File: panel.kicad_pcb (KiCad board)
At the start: 2 copper layers, 184.8 x 134.8 mm, 316 parts, among them J1 JST_SH_SM06B-SRSS-TB_1x06-1MP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, SW1 SW_Push, SW2 SW_Push, U1 M24C02-FMN

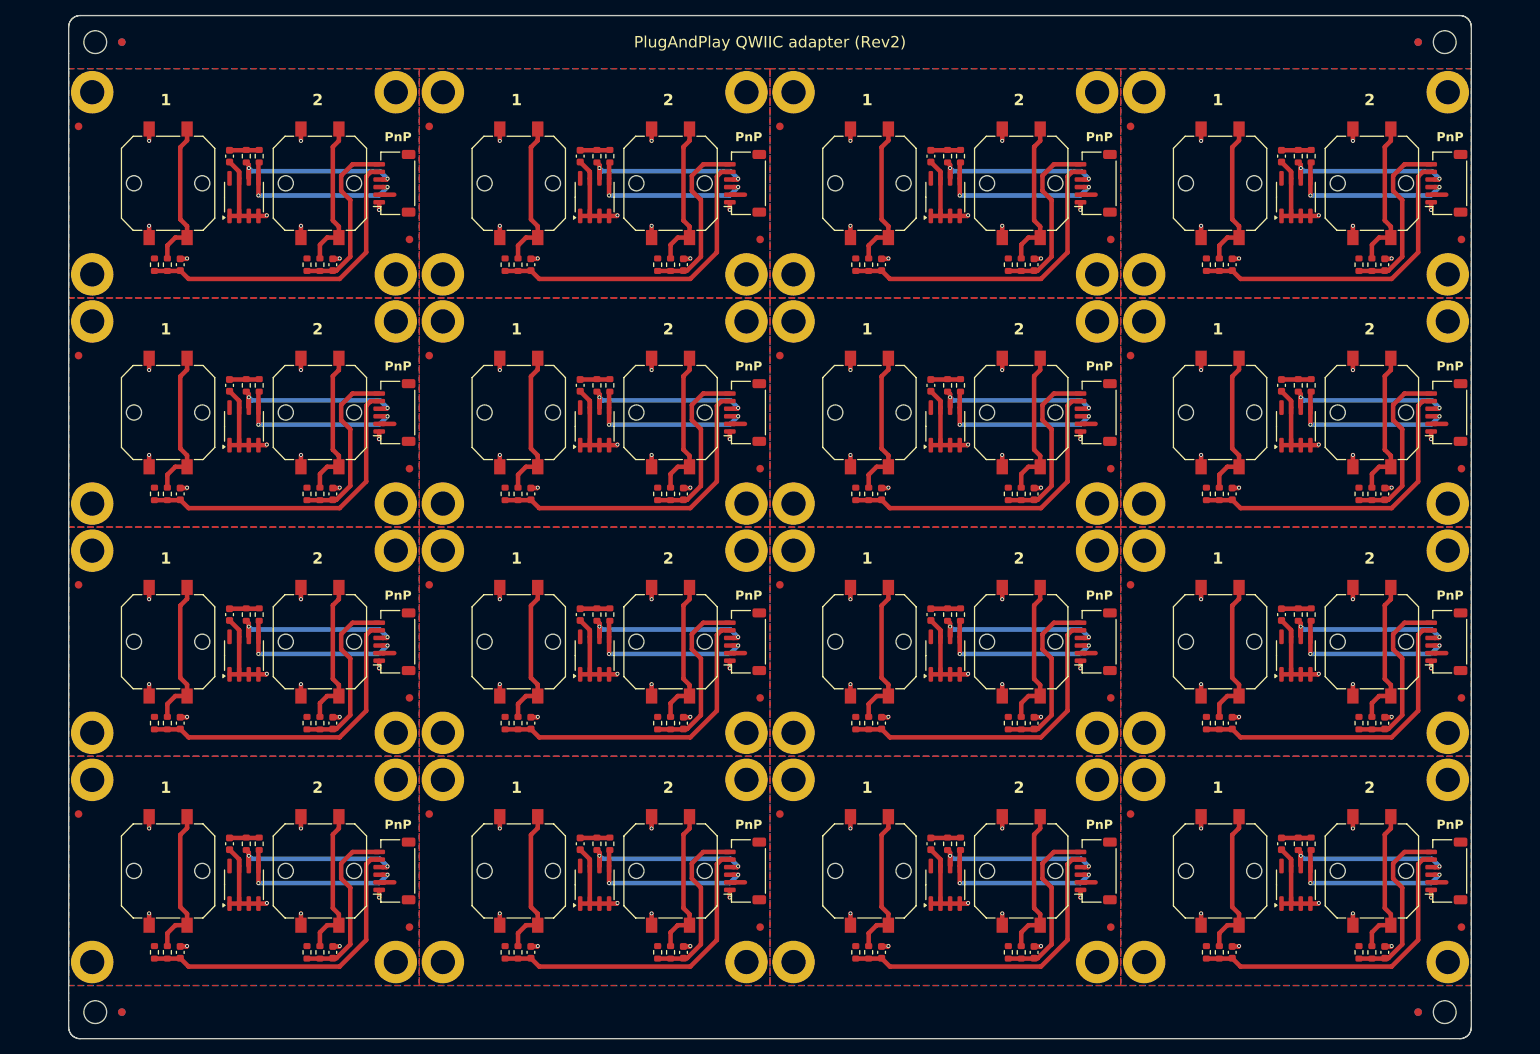
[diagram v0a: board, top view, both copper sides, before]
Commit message: Panel framing on all 4 sides
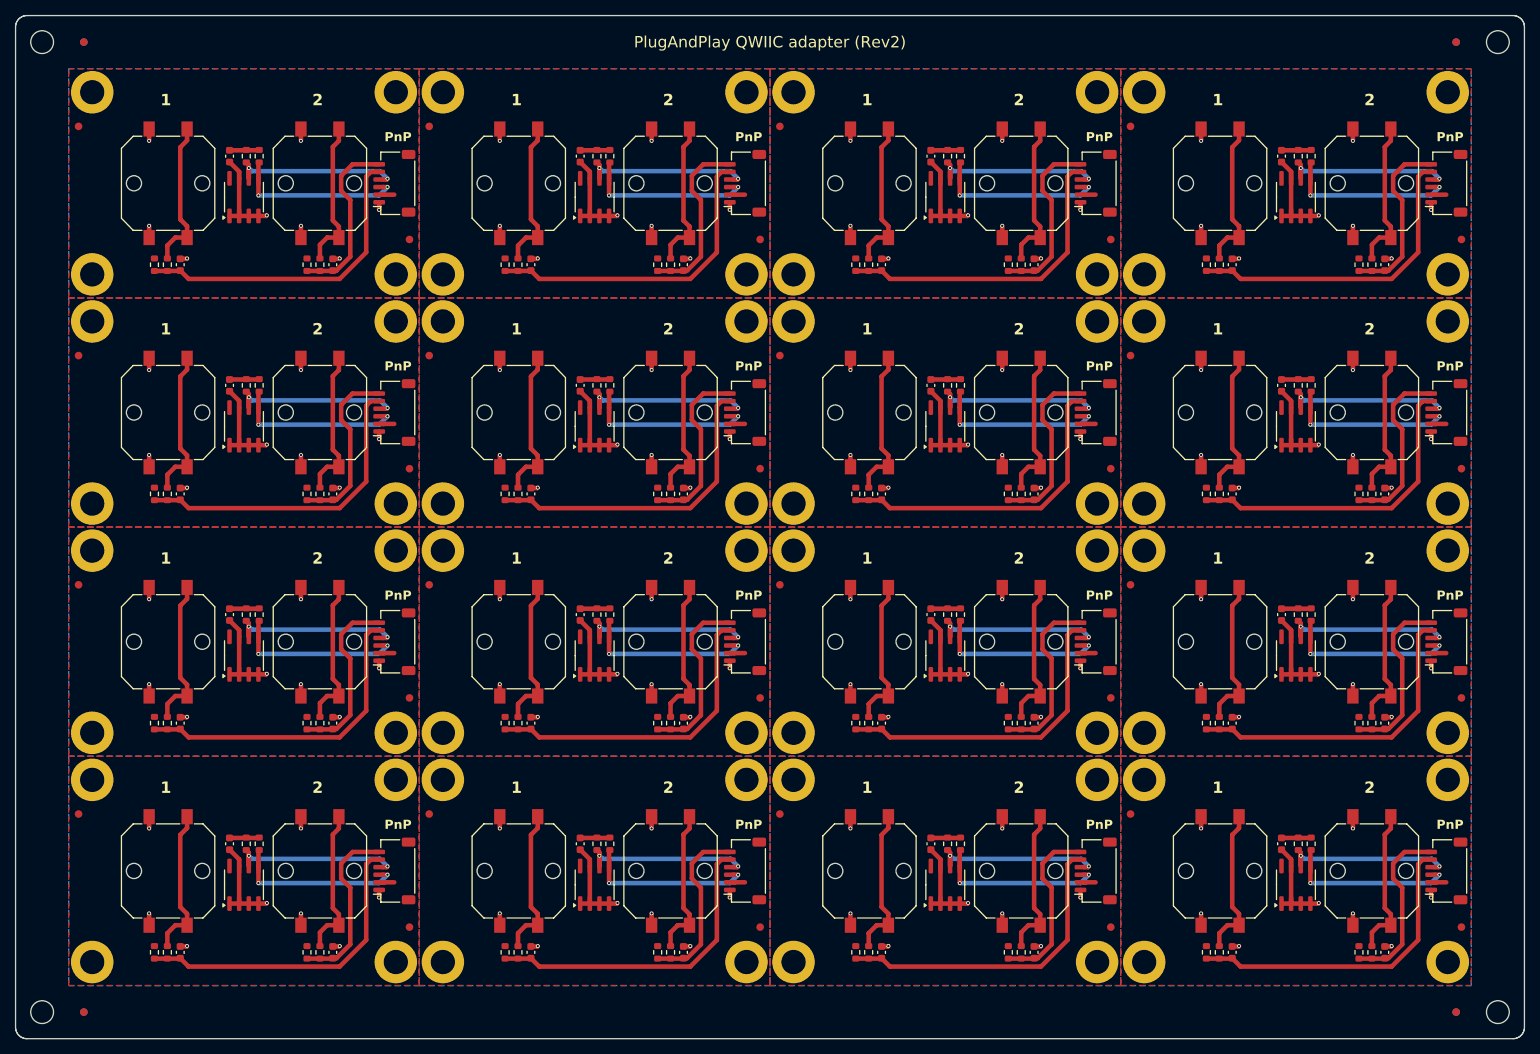
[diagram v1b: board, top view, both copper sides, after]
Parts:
- removed the C1 at (33.8, 98.9)
- removed the C1 at (126.2, 129.1)
- removed the C1 at (126.2, 38.5)
- removed the C1 at (80.0, 68.7)
- removed the C1 at (172.4, 129.1)
- removed the C1 at (172.4, 38.5)
- removed the C1 at (172.4, 68.7)
- removed the C1 at (172.4, 98.9)
- removed the C1 at (80.0, 98.9)
- removed the C1 at (33.8, 38.5)
- removed the C1 at (80.0, 38.5)
- removed the C1 at (126.2, 98.9)
- removed the C1 at (33.8, 129.1)
- removed the C1 at (126.2, 68.7)
- removed the C1 at (33.8, 68.7)
- removed the C1 at (80.0, 129.1)
- removed the C2 at (93.6, 143.4)
- removed the C2 at (93.6, 83.0)
- removed the C2 at (47.4, 83.0)
- removed the C2 at (186.0, 83.0)
- removed the C2 at (93.6, 113.2)
- removed the C2 at (139.8, 83.0)
- removed the C2 at (186.0, 143.4)
- removed the C2 at (47.4, 52.8)
- removed the C2 at (139.8, 113.2)
- removed the C2 at (47.4, 113.2)
- removed the C2 at (47.4, 143.4)
- removed the C2 at (139.8, 52.8)
- removed the C2 at (186.0, 113.2)
- removed the C2 at (93.6, 52.8)
- removed the C2 at (186.0, 52.8)
- removed the C2 at (139.8, 143.4)
- removed the C3 at (165.9, 143.4)
- removed the C3 at (165.9, 83.0)
- removed the C3 at (27.3, 143.4)
- removed the C3 at (27.3, 52.8)
- removed the C3 at (73.5, 52.8)
- removed the C3 at (165.9, 113.2)
- removed the C3 at (119.7, 83.0)
- removed the C3 at (27.3, 113.2)
- removed the C3 at (73.5, 113.2)
- removed the C3 at (73.5, 143.4)
- removed the C3 at (119.7, 143.4)
- removed the C3 at (73.5, 83.0)
- removed the C3 at (27.3, 83.0)
- removed the C3 at (119.7, 113.2)
- removed the C3 at (119.7, 52.8)
- removed the C3 at (165.9, 52.8)
- removed the J1 at (147.9, 102.5)
- removed the J1 at (101.7, 42.1)
- removed the J1 at (194.1, 132.7)
- removed the J1 at (101.7, 102.5)
- removed the J1 at (194.1, 102.5)
- removed the J1 at (55.5, 132.7)
- removed the J1 at (101.7, 72.3)
- removed the J1 at (194.1, 72.3)
- removed the J1 at (55.5, 42.1)
- removed the J1 at (194.1, 42.1)
- removed the J1 at (55.5, 102.5)
- removed the J1 at (147.9, 132.7)
- removed the J1 at (147.9, 72.3)
- removed the J1 at (147.9, 42.1)
- removed the J1 at (55.5, 72.3)
- removed the J1 at (101.7, 132.7)
- removed the R1 at (90.2, 52.8)
- removed the R1 at (136.4, 83.0)
- removed the R1 at (182.6, 113.2)
- removed the R1 at (44.0, 52.8)
- removed the R1 at (136.4, 52.8)
- removed the R1 at (136.4, 113.2)
- removed the R1 at (182.6, 83.0)
- removed the R1 at (44.0, 143.4)
- removed the R1 at (182.6, 52.8)
- removed the R1 at (44.0, 113.2)
- removed the R1 at (90.2, 113.2)
- removed the R1 at (182.6, 143.4)
- removed the R1 at (44.0, 83.0)
- removed the R1 at (136.4, 143.4)
- removed the R1 at (90.2, 143.4)
- removed the R1 at (90.2, 83.0)
- removed the R2 at (45.7, 113.2)
- removed the R2 at (138.1, 83.0)
- removed the R2 at (91.9, 143.4)
- removed the R2 at (45.7, 52.8)
- removed the R2 at (91.9, 52.8)
- removed the R2 at (184.3, 143.4)
- removed the R2 at (45.7, 143.4)
- removed the R2 at (184.3, 83.0)
- removed the R2 at (184.3, 113.2)
- removed the R2 at (138.1, 52.8)
- removed the R2 at (91.9, 83.0)
- removed the R2 at (184.3, 52.8)
- removed the R2 at (138.1, 113.2)
- removed the R2 at (45.7, 83.0)
- removed the R2 at (91.9, 113.2)
- removed the R2 at (138.1, 143.4)
- removed the R3 at (25.6, 113.2)
- removed the R3 at (164.2, 52.8)
- removed the R3 at (71.8, 143.4)
- removed the R3 at (118.0, 143.4)
- removed the R3 at (71.8, 113.2)
- removed the R3 at (164.2, 113.2)
- removed the R3 at (25.6, 83.0)
- removed the R3 at (164.2, 83.0)
- removed the R3 at (71.8, 83.0)
- removed the R3 at (25.6, 143.4)
- removed the R3 at (164.2, 143.4)
- removed the R3 at (25.6, 52.8)
- removed the R3 at (118.0, 83.0)
- removed the R3 at (118.0, 52.8)
- removed the R3 at (71.8, 52.8)
- removed the R3 at (118.0, 113.2)
- removed the R4 at (162.5, 143.4)
- removed the R4 at (70.1, 83.0)
- removed the R4 at (70.1, 143.4)
- removed the R4 at (70.1, 52.8)
- removed the R4 at (116.3, 83.0)
- removed the R4 at (70.1, 113.2)
- removed the R4 at (162.5, 83.0)
- removed the R4 at (116.3, 52.8)
- removed the R4 at (162.5, 52.8)
- removed the R4 at (162.5, 113.2)
- removed the R4 at (23.9, 83.0)
- removed the R4 at (23.9, 52.8)
- removed the R4 at (23.9, 143.4)
- removed the R4 at (23.9, 113.2)
- removed the R4 at (116.3, 113.2)
- removed the R4 at (116.3, 143.4)
- removed the R5 at (130.1, 68.7)
- removed the R5 at (37.7, 98.9)
- removed the R5 at (176.3, 68.7)
- removed the R5 at (83.9, 68.7)
- removed the R5 at (37.7, 68.7)
- removed the R5 at (83.9, 98.9)
- removed the R5 at (83.9, 38.5)
- removed the R5 at (37.7, 38.5)
- removed the R5 at (83.9, 129.1)
- removed the R5 at (130.1, 129.1)
- removed the R5 at (130.1, 98.9)
- removed the R5 at (37.7, 129.1)
- removed the R5 at (176.3, 129.1)
- removed the R5 at (176.3, 98.9)
- removed the R5 at (130.1, 38.5)
- removed the R5 at (176.3, 38.5)
- removed the R6 at (174.6, 98.9)
- removed the R6 at (174.6, 38.5)
- removed the R6 at (82.2, 38.5)
- removed the R6 at (36.0, 98.9)
- removed the R6 at (82.2, 98.9)
- removed the R6 at (174.6, 68.7)
- removed the R6 at (128.4, 68.7)
- removed the R6 at (36.0, 68.7)
- removed the R6 at (128.4, 129.1)
- removed the R6 at (36.0, 129.1)
- removed the R6 at (128.4, 98.9)
- removed the R6 at (82.2, 68.7)
- removed the R6 at (174.6, 129.1)
- removed the R6 at (36.0, 38.5)
- removed the R6 at (128.4, 38.5)
- removed the R6 at (82.2, 129.1)
- removed the REF** at (154.3, 60.3)
- removed the REF** at (15.7, 114.5)
- removed the REF** at (61.9, 84.3)
- removed the REF** at (152.5, 34.6)
- removed the REF** at (55.7, 90.5)
- removed the REF** at (108.1, 54.1)
- removed the REF** at (149.9, 79.7)
- removed the REF** at (194.3, 120.7)
- removed the REF** at (60.1, 34.6)
- removed the REF** at (154.3, 90.5)
- removed the REF** at (108.1, 30.1)
- removed the REF** at (148.1, 54.1)
- removed the REF** at (61.9, 60.3)
- removed the REF** at (148.1, 84.3)
- removed the REF** at (15.7, 90.5)
- removed the REF** at (152.5, 64.8)
- removed the REF** at (103.7, 109.9)
- removed the REF** at (101.9, 84.3)
- removed the REF** at (15.7, 60.3)
- removed the REF** at (60.1, 64.8)
- removed the REF** at (194.3, 90.5)
- removed the REF** at (148.1, 60.3)
- removed the REF** at (108.1, 144.7)
- removed the REF** at (103.7, 49.5)
- removed the REF** at (106.3, 125.2)
- removed the REF** at (13.9, 125.2)
- removed the REF** at (108.1, 90.5)
- removed the REF** at (61.9, 114.5)
- removed the REF** at (103.7, 140.1)
- removed the REF** at (194.3, 54.1)
- removed the REF** at (15.7, 120.7)
- removed the REF** at (154.3, 54.1)
- removed the REF** at (15.7, 30.1)
- removed the REF** at (57.5, 49.5)
- removed the REF** at (101.9, 54.1)
- removed the REF** at (196.1, 79.7)
- removed the REF** at (194.3, 84.3)
- removed the REF** at (194.3, 114.5)
- removed the REF** at (55.7, 84.3)
- removed the REF** at (149.9, 49.5)
- removed the REF** at (106.3, 95.0)
- removed the REF** at (15.7, 144.7)
- removed the REF** at (101.9, 30.1)
- removed the REF** at (108.1, 120.7)
- removed the REF** at (194.3, 60.3)
- removed the REF** at (60.1, 95.0)
- removed the REF** at (108.1, 84.3)
- removed the REF** at (55.7, 30.1)
- removed the REF** at (154.3, 30.1)
- removed the REF** at (196.1, 49.5)
- removed the REF** at (15.7, 54.1)
- removed the REF** at (55.7, 54.1)
- removed the REF** at (196.1, 140.1)
- removed the REF** at (101.9, 144.7)
- removed the REF** at (154.3, 120.7)
- removed the REF** at (13.9, 95.0)
- removed the REF** at (154.3, 144.7)
- removed the REF** at (61.9, 30.1)
- removed the REF** at (148.1, 144.7)
- removed the REF** at (148.1, 114.5)
- removed the REF** at (61.9, 90.5)
- removed the REF** at (57.5, 140.1)
- removed the REF** at (148.1, 90.5)
- removed the REF** at (13.9, 64.8)
- removed the REF** at (61.9, 54.1)
- removed the REF** at (101.9, 120.7)
- removed the REF** at (152.5, 95.0)
- removed the REF** at (148.1, 120.7)
- removed the REF** at (148.1, 30.1)
- removed the REF** at (152.5, 125.2)
- removed the REF** at (108.1, 60.3)
- removed the REF** at (61.9, 120.7)
- removed the REF** at (15.7, 84.3)
- removed the REF** at (101.9, 90.5)
- removed the REF** at (61.9, 144.7)
- removed the REF** at (194.3, 30.1)
- removed the REF** at (103.7, 79.7)
- removed the REF** at (55.7, 144.7)
- removed the REF** at (154.3, 114.5)
- removed the REF** at (55.7, 114.5)
- removed the REF** at (55.7, 60.3)
- removed the REF** at (101.9, 114.5)
- removed the REF** at (149.9, 109.9)
- removed the REF** at (55.7, 120.7)
- removed the REF** at (154.3, 84.3)
- removed the REF** at (106.3, 64.8)
- removed the REF** at (60.1, 125.2)
- removed the REF** at (13.9, 34.6)
- removed the REF** at (196.1, 109.9)
- removed the REF** at (106.3, 34.6)
- removed the REF** at (108.1, 114.5)
- removed the REF** at (57.5, 109.9)
- removed the REF** at (57.5, 79.7)
- removed the REF** at (149.9, 140.1)
- removed the REF** at (194.3, 144.7)
- removed the REF** at (101.9, 60.3)
- removed the SW1 at (25.7, 72.3)
- removed the SW1 at (118.1, 102.5)
- removed the SW1 at (164.3, 72.3)
- removed the SW1 at (118.1, 72.3)
- removed the SW1 at (164.3, 132.7)
- removed the SW1 at (71.9, 72.3)
- removed the SW1 at (164.3, 42.1)
- removed the SW1 at (118.1, 132.7)
- removed the SW1 at (25.7, 102.5)
- removed the SW1 at (164.3, 102.5)
- removed the SW1 at (71.9, 42.1)
- removed the SW1 at (71.9, 132.7)
- removed the SW1 at (118.1, 42.1)
- removed the SW1 at (25.7, 132.7)
- removed the SW1 at (71.9, 102.5)
- removed the SW1 at (25.7, 42.1)
- removed the SW2 at (91.9, 42.1)
- removed the SW2 at (138.1, 132.7)
- removed the SW2 at (45.7, 102.5)
- removed the SW2 at (45.7, 132.7)
- removed the SW2 at (184.3, 72.3)
- removed the SW2 at (138.1, 72.3)
- removed the SW2 at (184.3, 132.7)
- removed the SW2 at (45.7, 72.3)
- removed the SW2 at (138.1, 42.1)
- removed the SW2 at (184.3, 42.1)
- removed the SW2 at (91.9, 132.7)
- removed the SW2 at (184.3, 102.5)
- removed the SW2 at (91.9, 72.3)
- removed the SW2 at (91.9, 102.5)
- removed the SW2 at (45.7, 42.1)
- removed the SW2 at (138.1, 102.5)
- removed the U1 at (174.3, 134.5)
- removed the U1 at (35.7, 43.9)
- removed the U1 at (128.1, 43.9)
- removed the U1 at (81.9, 43.9)
- removed the U1 at (128.1, 104.3)
- removed the U1 at (35.7, 104.3)
- removed the U1 at (81.9, 104.3)
- removed the U1 at (128.1, 74.1)
- removed the U1 at (174.3, 74.1)
- removed the U1 at (128.1, 134.5)
- removed the U1 at (174.3, 104.3)
- removed the U1 at (81.9, 74.1)
- removed the U1 at (174.3, 43.9)
- removed the U1 at (35.7, 74.1)
- removed the U1 at (35.7, 134.5)
- removed the U1 at (81.9, 134.5)
- added C1: 0.1uF, Capacitor_SMD:C_0603_1608Metric, F.Cu at (80.0, 98.9)
- added C1: 0.1uF, Capacitor_SMD:C_0603_1608Metric, F.Cu at (80.0, 129.1)
- added C1: 0.1uF, Capacitor_SMD:C_0603_1608Metric, F.Cu at (33.8, 68.7)
- added C1: 0.1uF, Capacitor_SMD:C_0603_1608Metric, F.Cu at (126.2, 98.9)
- added C1: 0.1uF, Capacitor_SMD:C_0603_1608Metric, F.Cu at (80.0, 68.7)
- added C1: 0.1uF, Capacitor_SMD:C_0603_1608Metric, F.Cu at (33.8, 129.1)
- added C1: 0.1uF, Capacitor_SMD:C_0603_1608Metric, F.Cu at (126.2, 38.5)
- added C1: 0.1uF, Capacitor_SMD:C_0603_1608Metric, F.Cu at (172.4, 68.7)
- added C1: 0.1uF, Capacitor_SMD:C_0603_1608Metric, F.Cu at (126.2, 68.7)
- added C1: 0.1uF, Capacitor_SMD:C_0603_1608Metric, F.Cu at (172.4, 98.9)
- added C1: 0.1uF, Capacitor_SMD:C_0603_1608Metric, F.Cu at (33.8, 98.9)
- added C1: 0.1uF, Capacitor_SMD:C_0603_1608Metric, F.Cu at (172.4, 129.1)
- added C1: 0.1uF, Capacitor_SMD:C_0603_1608Metric, F.Cu at (80.0, 38.5)
- added C1: 0.1uF, Capacitor_SMD:C_0603_1608Metric, F.Cu at (33.8, 38.5)
- added C1: 0.1uF, Capacitor_SMD:C_0603_1608Metric, F.Cu at (126.2, 129.1)
- added C1: 0.1uF, Capacitor_SMD:C_0603_1608Metric, F.Cu at (172.4, 38.5)
- added C2: 0.1uF, Capacitor_SMD:C_0603_1608Metric, F.Cu at (186.0, 52.8)
- added C2: 0.1uF, Capacitor_SMD:C_0603_1608Metric, F.Cu at (93.6, 143.4)
- added C2: 0.1uF, Capacitor_SMD:C_0603_1608Metric, F.Cu at (139.8, 143.4)
- added C2: 0.1uF, Capacitor_SMD:C_0603_1608Metric, F.Cu at (93.6, 113.2)
- added C2: 0.1uF, Capacitor_SMD:C_0603_1608Metric, F.Cu at (139.8, 52.8)
- added C2: 0.1uF, Capacitor_SMD:C_0603_1608Metric, F.Cu at (186.0, 143.4)
- added C2: 0.1uF, Capacitor_SMD:C_0603_1608Metric, F.Cu at (139.8, 83.0)
- added C2: 0.1uF, Capacitor_SMD:C_0603_1608Metric, F.Cu at (47.4, 52.8)
- added C2: 0.1uF, Capacitor_SMD:C_0603_1608Metric, F.Cu at (47.4, 113.2)
- added C2: 0.1uF, Capacitor_SMD:C_0603_1608Metric, F.Cu at (93.6, 83.0)
- added C2: 0.1uF, Capacitor_SMD:C_0603_1608Metric, F.Cu at (139.8, 113.2)
- added C2: 0.1uF, Capacitor_SMD:C_0603_1608Metric, F.Cu at (47.4, 143.4)
- added C2: 0.1uF, Capacitor_SMD:C_0603_1608Metric, F.Cu at (186.0, 83.0)
- added C2: 0.1uF, Capacitor_SMD:C_0603_1608Metric, F.Cu at (47.4, 83.0)
- added C2: 0.1uF, Capacitor_SMD:C_0603_1608Metric, F.Cu at (186.0, 113.2)
- added C2: 0.1uF, Capacitor_SMD:C_0603_1608Metric, F.Cu at (93.6, 52.8)
- added C3: 0.1uF, Capacitor_SMD:C_0603_1608Metric, F.Cu at (119.7, 52.8)
- added C3: 0.1uF, Capacitor_SMD:C_0603_1608Metric, F.Cu at (27.3, 143.4)
- added C3: 0.1uF, Capacitor_SMD:C_0603_1608Metric, F.Cu at (165.9, 52.8)
- added C3: 0.1uF, Capacitor_SMD:C_0603_1608Metric, F.Cu at (73.5, 83.0)
- added C3: 0.1uF, Capacitor_SMD:C_0603_1608Metric, F.Cu at (165.9, 83.0)
- added C3: 0.1uF, Capacitor_SMD:C_0603_1608Metric, F.Cu at (73.5, 143.4)
- added C3: 0.1uF, Capacitor_SMD:C_0603_1608Metric, F.Cu at (119.7, 143.4)
- added C3: 0.1uF, Capacitor_SMD:C_0603_1608Metric, F.Cu at (27.3, 52.8)
- added C3: 0.1uF, Capacitor_SMD:C_0603_1608Metric, F.Cu at (165.9, 113.2)
- added C3: 0.1uF, Capacitor_SMD:C_0603_1608Metric, F.Cu at (73.5, 52.8)
- added C3: 0.1uF, Capacitor_SMD:C_0603_1608Metric, F.Cu at (27.3, 83.0)
- added C3: 0.1uF, Capacitor_SMD:C_0603_1608Metric, F.Cu at (119.7, 113.2)
- added C3: 0.1uF, Capacitor_SMD:C_0603_1608Metric, F.Cu at (73.5, 113.2)
- added C3: 0.1uF, Capacitor_SMD:C_0603_1608Metric, F.Cu at (165.9, 143.4)
- added C3: 0.1uF, Capacitor_SMD:C_0603_1608Metric, F.Cu at (27.3, 113.2)
- added C3: 0.1uF, Capacitor_SMD:C_0603_1608Metric, F.Cu at (119.7, 83.0)
- added J1: JST_SH_SM06B-SRSS-TB_1x06-1MP_P1.00mm_Horizontal, Connector_JST:JST_SH_SM06B-SRSS-TB_1x06-1MP_P1.00mm_Horizontal, F.Cu at (55.5, 42.1)
- added J1: JST_SH_SM06B-SRSS-TB_1x06-1MP_P1.00mm_Horizontal, Connector_JST:JST_SH_SM06B-SRSS-TB_1x06-1MP_P1.00mm_Horizontal, F.Cu at (194.1, 132.7)
- added J1: JST_SH_SM06B-SRSS-TB_1x06-1MP_P1.00mm_Horizontal, Connector_JST:JST_SH_SM06B-SRSS-TB_1x06-1MP_P1.00mm_Horizontal, F.Cu at (147.9, 72.3)
- added J1: JST_SH_SM06B-SRSS-TB_1x06-1MP_P1.00mm_Horizontal, Connector_JST:JST_SH_SM06B-SRSS-TB_1x06-1MP_P1.00mm_Horizontal, F.Cu at (194.1, 102.5)
- added J1: JST_SH_SM06B-SRSS-TB_1x06-1MP_P1.00mm_Horizontal, Connector_JST:JST_SH_SM06B-SRSS-TB_1x06-1MP_P1.00mm_Horizontal, F.Cu at (194.1, 72.3)
- added J1: JST_SH_SM06B-SRSS-TB_1x06-1MP_P1.00mm_Horizontal, Connector_JST:JST_SH_SM06B-SRSS-TB_1x06-1MP_P1.00mm_Horizontal, F.Cu at (147.9, 132.7)
- added J1: JST_SH_SM06B-SRSS-TB_1x06-1MP_P1.00mm_Horizontal, Connector_JST:JST_SH_SM06B-SRSS-TB_1x06-1MP_P1.00mm_Horizontal, F.Cu at (101.7, 72.3)
- added J1: JST_SH_SM06B-SRSS-TB_1x06-1MP_P1.00mm_Horizontal, Connector_JST:JST_SH_SM06B-SRSS-TB_1x06-1MP_P1.00mm_Horizontal, F.Cu at (147.9, 102.5)
- added J1: JST_SH_SM06B-SRSS-TB_1x06-1MP_P1.00mm_Horizontal, Connector_JST:JST_SH_SM06B-SRSS-TB_1x06-1MP_P1.00mm_Horizontal, F.Cu at (101.7, 132.7)
- added J1: JST_SH_SM06B-SRSS-TB_1x06-1MP_P1.00mm_Horizontal, Connector_JST:JST_SH_SM06B-SRSS-TB_1x06-1MP_P1.00mm_Horizontal, F.Cu at (101.7, 102.5)
- added J1: JST_SH_SM06B-SRSS-TB_1x06-1MP_P1.00mm_Horizontal, Connector_JST:JST_SH_SM06B-SRSS-TB_1x06-1MP_P1.00mm_Horizontal, F.Cu at (55.5, 132.7)
- added J1: JST_SH_SM06B-SRSS-TB_1x06-1MP_P1.00mm_Horizontal, Connector_JST:JST_SH_SM06B-SRSS-TB_1x06-1MP_P1.00mm_Horizontal, F.Cu at (55.5, 102.5)
- added J1: JST_SH_SM06B-SRSS-TB_1x06-1MP_P1.00mm_Horizontal, Connector_JST:JST_SH_SM06B-SRSS-TB_1x06-1MP_P1.00mm_Horizontal, F.Cu at (147.9, 42.1)
- added J1: JST_SH_SM06B-SRSS-TB_1x06-1MP_P1.00mm_Horizontal, Connector_JST:JST_SH_SM06B-SRSS-TB_1x06-1MP_P1.00mm_Horizontal, F.Cu at (55.5, 72.3)
- added J1: JST_SH_SM06B-SRSS-TB_1x06-1MP_P1.00mm_Horizontal, Connector_JST:JST_SH_SM06B-SRSS-TB_1x06-1MP_P1.00mm_Horizontal, F.Cu at (194.1, 42.1)
- added J1: JST_SH_SM06B-SRSS-TB_1x06-1MP_P1.00mm_Horizontal, Connector_JST:JST_SH_SM06B-SRSS-TB_1x06-1MP_P1.00mm_Horizontal, F.Cu at (101.7, 42.1)
- added R1: 10K, Resistor_SMD:R_0603_1608Metric, F.Cu at (182.6, 113.2)
- added R1: 10K, Resistor_SMD:R_0603_1608Metric, F.Cu at (44.0, 113.2)
- added R1: 10K, Resistor_SMD:R_0603_1608Metric, F.Cu at (44.0, 52.8)
- added R1: 10K, Resistor_SMD:R_0603_1608Metric, F.Cu at (44.0, 83.0)
- added R1: 10K, Resistor_SMD:R_0603_1608Metric, F.Cu at (44.0, 143.4)
- added R1: 10K, Resistor_SMD:R_0603_1608Metric, F.Cu at (136.4, 83.0)
- added R1: 10K, Resistor_SMD:R_0603_1608Metric, F.Cu at (136.4, 143.4)
- added R1: 10K, Resistor_SMD:R_0603_1608Metric, F.Cu at (90.2, 52.8)
- added R1: 10K, Resistor_SMD:R_0603_1608Metric, F.Cu at (90.2, 113.2)
- added R1: 10K, Resistor_SMD:R_0603_1608Metric, F.Cu at (182.6, 143.4)
- added R1: 10K, Resistor_SMD:R_0603_1608Metric, F.Cu at (90.2, 83.0)
- added R1: 10K, Resistor_SMD:R_0603_1608Metric, F.Cu at (136.4, 113.2)
- added R1: 10K, Resistor_SMD:R_0603_1608Metric, F.Cu at (182.6, 52.8)
- added R1: 10K, Resistor_SMD:R_0603_1608Metric, F.Cu at (182.6, 83.0)
- added R1: 10K, Resistor_SMD:R_0603_1608Metric, F.Cu at (90.2, 143.4)
- added R1: 10K, Resistor_SMD:R_0603_1608Metric, F.Cu at (136.4, 52.8)
- added R2: 1K, Resistor_SMD:R_0603_1608Metric, F.Cu at (91.9, 83.0)
- added R2: 1K, Resistor_SMD:R_0603_1608Metric, F.Cu at (184.3, 143.4)
- added R2: 1K, Resistor_SMD:R_0603_1608Metric, F.Cu at (138.1, 83.0)
- added R2: 1K, Resistor_SMD:R_0603_1608Metric, F.Cu at (138.1, 113.2)
- added R2: 1K, Resistor_SMD:R_0603_1608Metric, F.Cu at (184.3, 83.0)
- added R2: 1K, Resistor_SMD:R_0603_1608Metric, F.Cu at (91.9, 143.4)
- added R2: 1K, Resistor_SMD:R_0603_1608Metric, F.Cu at (45.7, 52.8)
- added R2: 1K, Resistor_SMD:R_0603_1608Metric, F.Cu at (45.7, 143.4)
- added R2: 1K, Resistor_SMD:R_0603_1608Metric, F.Cu at (138.1, 143.4)
- added R2: 1K, Resistor_SMD:R_0603_1608Metric, F.Cu at (138.1, 52.8)
- added R2: 1K, Resistor_SMD:R_0603_1608Metric, F.Cu at (91.9, 113.2)
- added R2: 1K, Resistor_SMD:R_0603_1608Metric, F.Cu at (184.3, 113.2)
- added R2: 1K, Resistor_SMD:R_0603_1608Metric, F.Cu at (45.7, 113.2)
- added R2: 1K, Resistor_SMD:R_0603_1608Metric, F.Cu at (91.9, 52.8)
- added R2: 1K, Resistor_SMD:R_0603_1608Metric, F.Cu at (184.3, 52.8)
- added R2: 1K, Resistor_SMD:R_0603_1608Metric, F.Cu at (45.7, 83.0)
- added R3: 1K, Resistor_SMD:R_0603_1608Metric, F.Cu at (118.0, 83.0)
- added R3: 1K, Resistor_SMD:R_0603_1608Metric, F.Cu at (25.6, 52.8)
- added R3: 1K, Resistor_SMD:R_0603_1608Metric, F.Cu at (25.6, 83.0)
- added R3: 1K, Resistor_SMD:R_0603_1608Metric, F.Cu at (71.8, 113.2)
- added R3: 1K, Resistor_SMD:R_0603_1608Metric, F.Cu at (164.2, 143.4)
- added R3: 1K, Resistor_SMD:R_0603_1608Metric, F.Cu at (164.2, 52.8)
- added R3: 1K, Resistor_SMD:R_0603_1608Metric, F.Cu at (25.6, 143.4)
- added R3: 1K, Resistor_SMD:R_0603_1608Metric, F.Cu at (71.8, 52.8)
- added R3: 1K, Resistor_SMD:R_0603_1608Metric, F.Cu at (164.2, 113.2)
- added R3: 1K, Resistor_SMD:R_0603_1608Metric, F.Cu at (25.6, 113.2)
- added R3: 1K, Resistor_SMD:R_0603_1608Metric, F.Cu at (118.0, 113.2)
- added R3: 1K, Resistor_SMD:R_0603_1608Metric, F.Cu at (164.2, 83.0)
- added R3: 1K, Resistor_SMD:R_0603_1608Metric, F.Cu at (118.0, 52.8)
- added R3: 1K, Resistor_SMD:R_0603_1608Metric, F.Cu at (71.8, 143.4)
- added R3: 1K, Resistor_SMD:R_0603_1608Metric, F.Cu at (118.0, 143.4)
- added R3: 1K, Resistor_SMD:R_0603_1608Metric, F.Cu at (71.8, 83.0)
- added R4: 10K, Resistor_SMD:R_0603_1608Metric, F.Cu at (23.9, 83.0)
- added R4: 10K, Resistor_SMD:R_0603_1608Metric, F.Cu at (70.1, 143.4)
- added R4: 10K, Resistor_SMD:R_0603_1608Metric, F.Cu at (23.9, 143.4)
- added R4: 10K, Resistor_SMD:R_0603_1608Metric, F.Cu at (162.5, 52.8)
- added R4: 10K, Resistor_SMD:R_0603_1608Metric, F.Cu at (116.3, 143.4)
- added R4: 10K, Resistor_SMD:R_0603_1608Metric, F.Cu at (116.3, 83.0)
- added R4: 10K, Resistor_SMD:R_0603_1608Metric, F.Cu at (162.5, 113.2)
- added R4: 10K, Resistor_SMD:R_0603_1608Metric, F.Cu at (70.1, 83.0)
- added R4: 10K, Resistor_SMD:R_0603_1608Metric, F.Cu at (116.3, 113.2)
- added R4: 10K, Resistor_SMD:R_0603_1608Metric, F.Cu at (162.5, 143.4)
- added R4: 10K, Resistor_SMD:R_0603_1608Metric, F.Cu at (23.9, 52.8)
- added R4: 10K, Resistor_SMD:R_0603_1608Metric, F.Cu at (162.5, 83.0)
- added R4: 10K, Resistor_SMD:R_0603_1608Metric, F.Cu at (70.1, 52.8)
- added R4: 10K, Resistor_SMD:R_0603_1608Metric, F.Cu at (23.9, 113.2)
- added R4: 10K, Resistor_SMD:R_0603_1608Metric, F.Cu at (116.3, 52.8)
- added R4: 10K, Resistor_SMD:R_0603_1608Metric, F.Cu at (70.1, 113.2)
- added R5: 2.2K, Resistor_SMD:R_0603_1608Metric, F.Cu at (176.3, 98.9)
- added R5: 2.2K, Resistor_SMD:R_0603_1608Metric, F.Cu at (83.9, 68.7)
- added R5: 2.2K, Resistor_SMD:R_0603_1608Metric, F.Cu at (130.1, 68.7)
- added R5: 2.2K, Resistor_SMD:R_0603_1608Metric, F.Cu at (83.9, 38.5)
- added R5: 2.2K, Resistor_SMD:R_0603_1608Metric, F.Cu at (83.9, 129.1)
- added R5: 2.2K, Resistor_SMD:R_0603_1608Metric, F.Cu at (37.7, 68.7)
- added R5: 2.2K, Resistor_SMD:R_0603_1608Metric, F.Cu at (37.7, 38.5)
- added R5: 2.2K, Resistor_SMD:R_0603_1608Metric, F.Cu at (176.3, 68.7)
- added R5: 2.2K, Resistor_SMD:R_0603_1608Metric, F.Cu at (130.1, 98.9)
- added R5: 2.2K, Resistor_SMD:R_0603_1608Metric, F.Cu at (83.9, 98.9)
- added R5: 2.2K, Resistor_SMD:R_0603_1608Metric, F.Cu at (176.3, 38.5)
- added R5: 2.2K, Resistor_SMD:R_0603_1608Metric, F.Cu at (130.1, 129.1)
- added R5: 2.2K, Resistor_SMD:R_0603_1608Metric, F.Cu at (130.1, 38.5)
- added R5: 2.2K, Resistor_SMD:R_0603_1608Metric, F.Cu at (37.7, 98.9)
- added R5: 2.2K, Resistor_SMD:R_0603_1608Metric, F.Cu at (37.7, 129.1)
- added R5: 2.2K, Resistor_SMD:R_0603_1608Metric, F.Cu at (176.3, 129.1)
- added R6: 2.2K, Resistor_SMD:R_0603_1608Metric, F.Cu at (82.2, 38.5)
- added R6: 2.2K, Resistor_SMD:R_0603_1608Metric, F.Cu at (174.6, 98.9)
- added R6: 2.2K, Resistor_SMD:R_0603_1608Metric, F.Cu at (36.0, 38.5)
- added R6: 2.2K, Resistor_SMD:R_0603_1608Metric, F.Cu at (128.4, 129.1)
- added R6: 2.2K, Resistor_SMD:R_0603_1608Metric, F.Cu at (82.2, 98.9)
- added R6: 2.2K, Resistor_SMD:R_0603_1608Metric, F.Cu at (36.0, 129.1)
- added R6: 2.2K, Resistor_SMD:R_0603_1608Metric, F.Cu at (36.0, 68.7)
- added R6: 2.2K, Resistor_SMD:R_0603_1608Metric, F.Cu at (174.6, 68.7)
- added R6: 2.2K, Resistor_SMD:R_0603_1608Metric, F.Cu at (82.2, 68.7)
- added R6: 2.2K, Resistor_SMD:R_0603_1608Metric, F.Cu at (36.0, 98.9)
- added R6: 2.2K, Resistor_SMD:R_0603_1608Metric, F.Cu at (174.6, 38.5)
- added R6: 2.2K, Resistor_SMD:R_0603_1608Metric, F.Cu at (128.4, 68.7)
- added R6: 2.2K, Resistor_SMD:R_0603_1608Metric, F.Cu at (128.4, 98.9)
- added R6: 2.2K, Resistor_SMD:R_0603_1608Metric, F.Cu at (174.6, 129.1)
- added R6: 2.2K, Resistor_SMD:R_0603_1608Metric, F.Cu at (128.4, 38.5)
- added R6: 2.2K, Resistor_SMD:R_0603_1608Metric, F.Cu at (82.2, 129.1)
- added REF**: MountingHole_3.2mm_M3_DIN965_Pad, MountingHole:MountingHole_3.2mm_M3_DIN965_Pad, F.Cu at (148.1, 120.7)
- added REF**: Fiducial_1mm_Mask2mm, Fiducial:Fiducial_1mm_Mask2mm, F.Cu at (196.1, 49.5)
- added REF**: Fiducial_1mm_Mask2mm, Fiducial:Fiducial_1mm_Mask2mm, F.Cu at (149.9, 49.5)
- added REF**: Fiducial_1mm_Mask2mm, Fiducial:Fiducial_1mm_Mask2mm, F.Cu at (106.3, 34.6)
- added REF**: MountingHole_3.2mm_M3_DIN965_Pad, MountingHole:MountingHole_3.2mm_M3_DIN965_Pad, F.Cu at (108.1, 114.5)
- added REF**: MountingHole_3.2mm_M3_DIN965_Pad, MountingHole:MountingHole_3.2mm_M3_DIN965_Pad, F.Cu at (194.3, 120.7)
- added REF**: MountingHole_3.2mm_M3_DIN965_Pad, MountingHole:MountingHole_3.2mm_M3_DIN965_Pad, F.Cu at (55.7, 60.3)
- added REF**: MountingHole_3.2mm_M3_DIN965_Pad, MountingHole:MountingHole_3.2mm_M3_DIN965_Pad, F.Cu at (15.7, 144.7)
- added REF**: Fiducial_1mm_Mask2mm, Fiducial:Fiducial_1mm_Mask2mm, F.Cu at (196.1, 140.1)
- added REF**: MountingHole_3.2mm_M3_DIN965_Pad, MountingHole:MountingHole_3.2mm_M3_DIN965_Pad, F.Cu at (61.9, 54.1)
- added REF**: MountingHole_3.2mm_M3_DIN965_Pad, MountingHole:MountingHole_3.2mm_M3_DIN965_Pad, F.Cu at (55.7, 144.7)
- added REF**: MountingHole_3.2mm_M3_DIN965_Pad, MountingHole:MountingHole_3.2mm_M3_DIN965_Pad, F.Cu at (194.3, 84.3)
- added REF**: Fiducial_1mm_Mask2mm, Fiducial:Fiducial_1mm_Mask2mm, F.Cu at (152.5, 64.8)
- added REF**: Fiducial_1mm_Mask2mm, Fiducial:Fiducial_1mm_Mask2mm, F.Cu at (106.3, 95.0)
- added REF**: MountingHole_3.2mm_M3_DIN965_Pad, MountingHole:MountingHole_3.2mm_M3_DIN965_Pad, F.Cu at (108.1, 90.5)
- added REF**: Fiducial_1mm_Mask2mm, Fiducial:Fiducial_1mm_Mask2mm, F.Cu at (152.5, 34.6)
- added REF**: Fiducial_1mm_Mask2mm, Fiducial:Fiducial_1mm_Mask2mm, F.Cu at (13.9, 95.0)
- added REF**: MountingHole_3.2mm_M3_DIN965_Pad, MountingHole:MountingHole_3.2mm_M3_DIN965_Pad, F.Cu at (194.3, 30.1)
- added REF**: Fiducial_1mm_Mask2mm, Fiducial:Fiducial_1mm_Mask2mm, F.Cu at (60.1, 64.8)
- added REF**: Fiducial_1mm_Mask2mm, Fiducial:Fiducial_1mm_Mask2mm, F.Cu at (60.1, 95.0)
- added REF**: MountingHole_3.2mm_M3_DIN965_Pad, MountingHole:MountingHole_3.2mm_M3_DIN965_Pad, F.Cu at (154.3, 90.5)
- added REF**: MountingHole_3.2mm_M3_DIN965_Pad, MountingHole:MountingHole_3.2mm_M3_DIN965_Pad, F.Cu at (148.1, 114.5)
- added REF**: MountingHole_3.2mm_M3_DIN965_Pad, MountingHole:MountingHole_3.2mm_M3_DIN965_Pad, F.Cu at (101.9, 120.7)
- added REF**: MountingHole_3.2mm_M3_DIN965_Pad, MountingHole:MountingHole_3.2mm_M3_DIN965_Pad, F.Cu at (194.3, 90.5)
- added REF**: Fiducial_1mm_Mask2mm, Fiducial:Fiducial_1mm_Mask2mm, F.Cu at (149.9, 79.7)
- added REF**: Fiducial_1mm_Mask2mm, Fiducial:Fiducial_1mm_Mask2mm, F.Cu at (13.9, 125.2)
- added REF**: Fiducial_1mm_Mask2mm, Fiducial:Fiducial_1mm_Mask2mm, F.Cu at (196.1, 109.9)
- added REF**: MountingHole_3.2mm_M3_DIN965_Pad, MountingHole:MountingHole_3.2mm_M3_DIN965_Pad, F.Cu at (15.7, 90.5)
- added REF**: MountingHole_3.2mm_M3_DIN965_Pad, MountingHole:MountingHole_3.2mm_M3_DIN965_Pad, F.Cu at (154.3, 144.7)
- added REF**: MountingHole_3.2mm_M3_DIN965_Pad, MountingHole:MountingHole_3.2mm_M3_DIN965_Pad, F.Cu at (61.9, 144.7)
- added REF**: MountingHole_3.2mm_M3_DIN965_Pad, MountingHole:MountingHole_3.2mm_M3_DIN965_Pad, F.Cu at (148.1, 60.3)
- added REF**: MountingHole_3.2mm_M3_DIN965_Pad, MountingHole:MountingHole_3.2mm_M3_DIN965_Pad, F.Cu at (15.7, 84.3)
- added REF**: MountingHole_3.2mm_M3_DIN965_Pad, MountingHole:MountingHole_3.2mm_M3_DIN965_Pad, F.Cu at (101.9, 30.1)
- added REF**: Fiducial_1mm_Mask2mm, Fiducial:Fiducial_1mm_Mask2mm, F.Cu at (103.7, 140.1)
- added REF**: Fiducial_1mm_Mask2mm, Fiducial:Fiducial_1mm_Mask2mm, F.Cu at (149.9, 109.9)
- added REF**: MountingHole_3.2mm_M3_DIN965_Pad, MountingHole:MountingHole_3.2mm_M3_DIN965_Pad, F.Cu at (154.3, 60.3)
- added REF**: Fiducial_1mm_Mask2mm, Fiducial:Fiducial_1mm_Mask2mm, F.Cu at (60.1, 125.2)
- added REF**: MountingHole_3.2mm_M3_DIN965_Pad, MountingHole:MountingHole_3.2mm_M3_DIN965_Pad, F.Cu at (15.7, 114.5)
- added REF**: MountingHole_3.2mm_M3_DIN965_Pad, MountingHole:MountingHole_3.2mm_M3_DIN965_Pad, F.Cu at (148.1, 90.5)
- added REF**: MountingHole_3.2mm_M3_DIN965_Pad, MountingHole:MountingHole_3.2mm_M3_DIN965_Pad, F.Cu at (154.3, 54.1)
- added REF**: MountingHole_3.2mm_M3_DIN965_Pad, MountingHole:MountingHole_3.2mm_M3_DIN965_Pad, F.Cu at (194.3, 60.3)
- added REF**: Fiducial_1mm_Mask2mm, Fiducial:Fiducial_1mm_Mask2mm, F.Cu at (106.3, 64.8)
- added REF**: Fiducial_1mm_Mask2mm, Fiducial:Fiducial_1mm_Mask2mm, F.Cu at (57.5, 140.1)
- added REF**: Fiducial_1mm_Mask2mm, Fiducial:Fiducial_1mm_Mask2mm, F.Cu at (103.7, 49.5)
- added REF**: MountingHole_3.2mm_M3_DIN965_Pad, MountingHole:MountingHole_3.2mm_M3_DIN965_Pad, F.Cu at (148.1, 30.1)
- added REF**: MountingHole_3.2mm_M3_DIN965_Pad, MountingHole:MountingHole_3.2mm_M3_DIN965_Pad, F.Cu at (154.3, 120.7)
- added REF**: MountingHole_3.2mm_M3_DIN965_Pad, MountingHole:MountingHole_3.2mm_M3_DIN965_Pad, F.Cu at (148.1, 84.3)
- added REF**: MountingHole_3.2mm_M3_DIN965_Pad, MountingHole:MountingHole_3.2mm_M3_DIN965_Pad, F.Cu at (101.9, 114.5)
- added REF**: MountingHole_3.2mm_M3_DIN965_Pad, MountingHole:MountingHole_3.2mm_M3_DIN965_Pad, F.Cu at (101.9, 60.3)
- added REF**: MountingHole_3.2mm_M3_DIN965_Pad, MountingHole:MountingHole_3.2mm_M3_DIN965_Pad, F.Cu at (55.7, 30.1)
- added REF**: MountingHole_3.2mm_M3_DIN965_Pad, MountingHole:MountingHole_3.2mm_M3_DIN965_Pad, F.Cu at (108.1, 120.7)
- added REF**: MountingHole_3.2mm_M3_DIN965_Pad, MountingHole:MountingHole_3.2mm_M3_DIN965_Pad, F.Cu at (15.7, 60.3)
- added REF**: Fiducial_1mm_Mask2mm, Fiducial:Fiducial_1mm_Mask2mm, F.Cu at (149.9, 140.1)
- added REF**: MountingHole_3.2mm_M3_DIN965_Pad, MountingHole:MountingHole_3.2mm_M3_DIN965_Pad, F.Cu at (55.7, 54.1)
- added REF**: MountingHole_3.2mm_M3_DIN965_Pad, MountingHole:MountingHole_3.2mm_M3_DIN965_Pad, F.Cu at (61.9, 60.3)
- added REF**: MountingHole_3.2mm_M3_DIN965_Pad, MountingHole:MountingHole_3.2mm_M3_DIN965_Pad, F.Cu at (148.1, 144.7)
- added REF**: MountingHole_3.2mm_M3_DIN965_Pad, MountingHole:MountingHole_3.2mm_M3_DIN965_Pad, F.Cu at (108.1, 54.1)
- added REF**: MountingHole_3.2mm_M3_DIN965_Pad, MountingHole:MountingHole_3.2mm_M3_DIN965_Pad, F.Cu at (108.1, 60.3)
- added REF**: MountingHole_3.2mm_M3_DIN965_Pad, MountingHole:MountingHole_3.2mm_M3_DIN965_Pad, F.Cu at (61.9, 90.5)
- added REF**: MountingHole_3.2mm_M3_DIN965_Pad, MountingHole:MountingHole_3.2mm_M3_DIN965_Pad, F.Cu at (108.1, 144.7)
- added REF**: MountingHole_3.2mm_M3_DIN965_Pad, MountingHole:MountingHole_3.2mm_M3_DIN965_Pad, F.Cu at (194.3, 54.1)
- added REF**: MountingHole_3.2mm_M3_DIN965_Pad, MountingHole:MountingHole_3.2mm_M3_DIN965_Pad, F.Cu at (148.1, 54.1)
- added REF**: MountingHole_3.2mm_M3_DIN965_Pad, MountingHole:MountingHole_3.2mm_M3_DIN965_Pad, F.Cu at (55.7, 120.7)
- added REF**: Fiducial_1mm_Mask2mm, Fiducial:Fiducial_1mm_Mask2mm, F.Cu at (103.7, 79.7)
- added REF**: MountingHole_3.2mm_M3_DIN965_Pad, MountingHole:MountingHole_3.2mm_M3_DIN965_Pad, F.Cu at (154.3, 30.1)
- added REF**: MountingHole_3.2mm_M3_DIN965_Pad, MountingHole:MountingHole_3.2mm_M3_DIN965_Pad, F.Cu at (194.3, 144.7)
- added REF**: MountingHole_3.2mm_M3_DIN965_Pad, MountingHole:MountingHole_3.2mm_M3_DIN965_Pad, F.Cu at (108.1, 30.1)
- added REF**: MountingHole_3.2mm_M3_DIN965_Pad, MountingHole:MountingHole_3.2mm_M3_DIN965_Pad, F.Cu at (108.1, 84.3)
- added REF**: MountingHole_3.2mm_M3_DIN965_Pad, MountingHole:MountingHole_3.2mm_M3_DIN965_Pad, F.Cu at (55.7, 90.5)
- added REF**: MountingHole_3.2mm_M3_DIN965_Pad, MountingHole:MountingHole_3.2mm_M3_DIN965_Pad, F.Cu at (61.9, 84.3)
- added REF**: Fiducial_1mm_Mask2mm, Fiducial:Fiducial_1mm_Mask2mm, F.Cu at (152.5, 95.0)
- added REF**: Fiducial_1mm_Mask2mm, Fiducial:Fiducial_1mm_Mask2mm, F.Cu at (60.1, 34.6)
- added REF**: MountingHole_3.2mm_M3_DIN965_Pad, MountingHole:MountingHole_3.2mm_M3_DIN965_Pad, F.Cu at (101.9, 84.3)
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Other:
- board size 184.8 x 134.8 mm -> 198.8 x 134.8 mm

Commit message: Changing the button names on silk level to 0 and 1
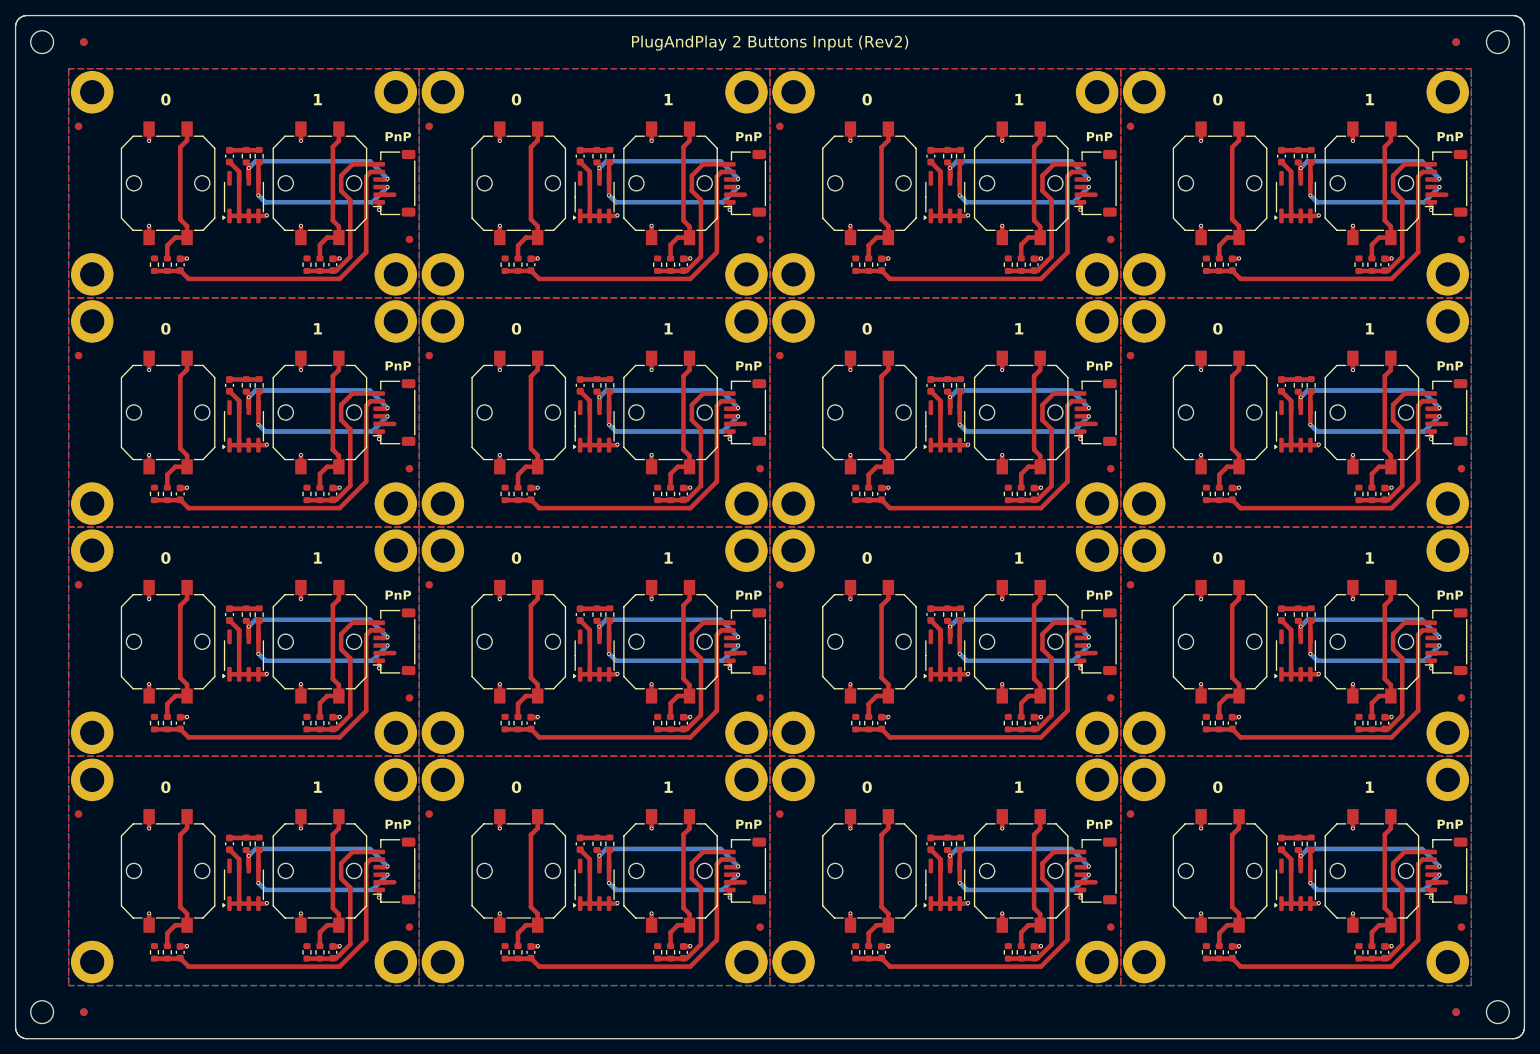
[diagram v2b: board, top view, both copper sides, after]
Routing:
- net Board_9-SCL: track 23.2 -> 23.9 mm
- net Board_8-SDA: track 22.5 -> 23.3 mm
- net Board_11-SCL: track 23.2 -> 23.9 mm
- net Board_8-SCL: track 23.2 -> 23.9 mm
- net Board_3-SCL: track 23.2 -> 23.9 mm
- net Board_11-SDA: track 22.5 -> 23.3 mm
- net Board_10-SDA: track 22.5 -> 23.3 mm
- net Board_10-SCL: track 23.2 -> 23.9 mm
- net Board_9-SDA: track 22.5 -> 23.3 mm
- net Board_0-SDA: track 22.5 -> 23.3 mm
- net Board_3-SDA: track 22.5 -> 23.3 mm
- net Board_2-SDA: track 22.5 -> 23.3 mm
- net Board_2-SCL: track 23.2 -> 23.9 mm
- net Board_1-SDA: track 22.5 -> 23.3 mm
- net Board_1-SCL: track 23.2 -> 23.9 mm
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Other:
- board text added: "0"
- board text added: "PlugAndPlay 2 Buttons Input (Rev2)"
- board text removed: "2"
- board text removed: "PlugAndPlay QWIIC adapter (Rev2)"
